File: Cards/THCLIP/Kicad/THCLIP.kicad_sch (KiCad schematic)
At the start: 12 parts, among them J2 Conn_01x03_Pin, J3 Conn_01x05_Pin, K1 Relay_SPDT, U1 RS3K-2424S/H3

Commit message: updated process description more
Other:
- note added: "Process ------- Recieve input height sensing enable signal Activate dc-dc converter - 24V DC will appear on the dc-dc converter output - A small current will flow through via 100 kOhm resistor (shorted output) - Relay will activate - Connection between work piece ground and torch shield ground is broken - Output will be unshorted, current through resistor stops flowing - 23V voltage appears betwe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"
- note removed: "Process ------- Recieve input height sensing signal Activate dc-dc converter - 24V DC will appear on the dc-dc converter output - A small current will flow through via 100 kOhm resistor (shorted output) - Relay will activate - Connection between work piece ground and torch shield ground is broken - Output will be unshorted, current through resistor stops flowing - 23V voltage appears between elec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"
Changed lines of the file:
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@@
 		)
 	)
-	(text "Process\n-------\nRecieve input height sensing signal\nActivate dc-dc converter\n	- 24V DC will appear on the dc-dc converter output\n	- A small current will flow through via 100 kOhm resistor (shorted output)\n	- Relay will activate\n		- Connection between work piece ground and torch shield ground is broken\n		- Output will be unshorted, current through resistor stops flowing\n		- 23V voltage appears between electrode and work piece ground\nWait a few tenths of a second to allow relay to settle before monitoring gap voltage\nWhen Arc voltage < x V: raise contact Signal\nLoss of height sensing signal: exit sensing mode, lower contact Signal\n\n"
+	(text "Process\n-------\nRecieve input height sensing enable signal\nActivate dc-dc converter\n	- 24V DC will appear on the dc-dc converter output\n	- A small current will flow through via 100 kOhm resistor (shorted output)\n	- Relay will activate\n		- Connection between work piece ground and torch shield ground is broken\n		- Output will be unshorted, current through resistor stops flowing\n		- 23V voltage appears between electrode and work piece ground, gap voltage\nWait for gap voltage to go above limit voltage. Needed for relay to settle (some milliseconds)\nWhen gap voltage goes back below limit voltage, that is contact, raise sensed/contact flag\nLoss of enable signal: exit sensing mode, lower contact Signal\n\n"
 		(exclude_from_sim no)
-		(at 88.646 131.826 0)
+		(at 90.424 131.826 0)
 		(effects
 			(font

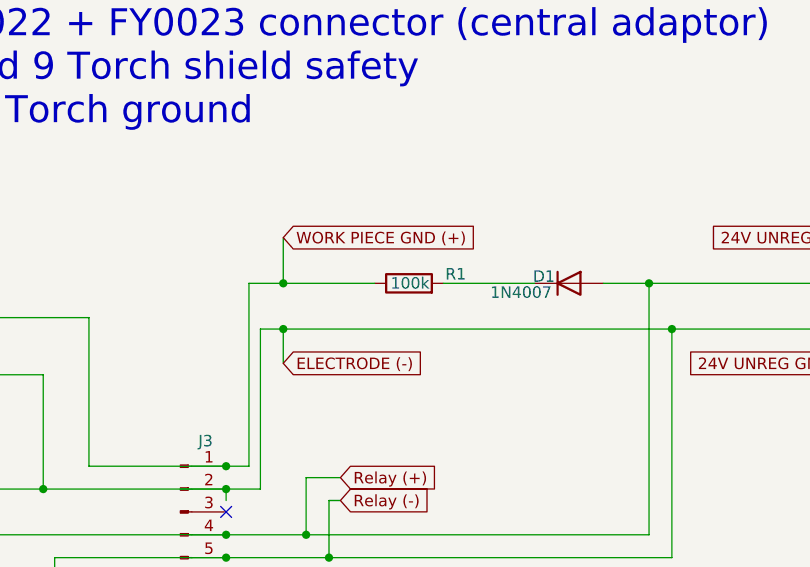
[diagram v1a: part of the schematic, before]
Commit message: Updated short-circuit resistor to 4k7 for more stable voltage.
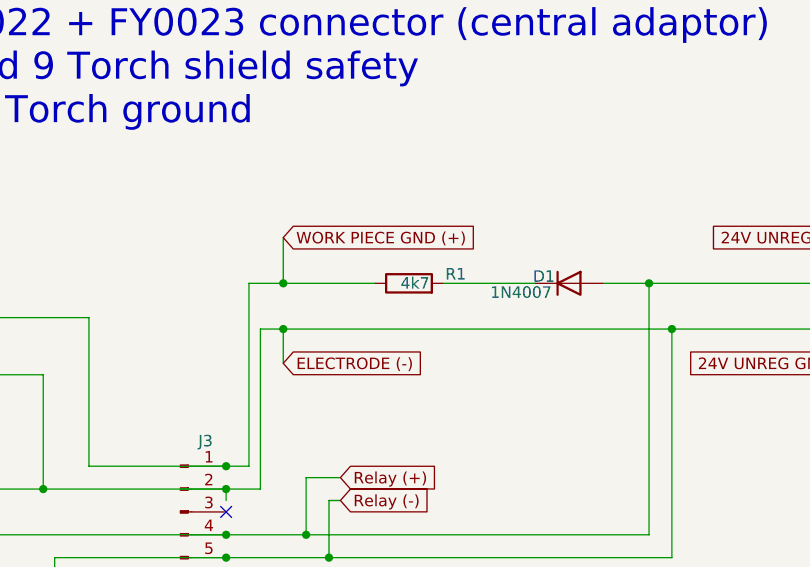
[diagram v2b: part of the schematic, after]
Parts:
- R1: value 100k -> 4k7; footprint Resistor_SMD:R_2512_6332Metric_Pad1.40x3.35mm_HandSolder -> Resistor_THT:R_Axial_DIN0207_L6.3mm_D2.5mm_P10.16mm_Horizontal
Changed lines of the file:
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@@
 			)
 		)
-		(property "Value" "100k"
+		(property "Value" "4k7"
 			(at 152.146 55.88 90)
 			(effects
@@
 			)
 		)
-		(property "Footprint" "Resistor_SMD:R_2512_6332Metric_Pad1.40x3.35mm_HandSolder"
+		(property "Footprint" "Resistor_THT:R_Axial_DIN0207_L6.3mm_D2.5mm_P10.16mm_Horizontal"
 			(at 149.86 57.658 90)
 			(effects

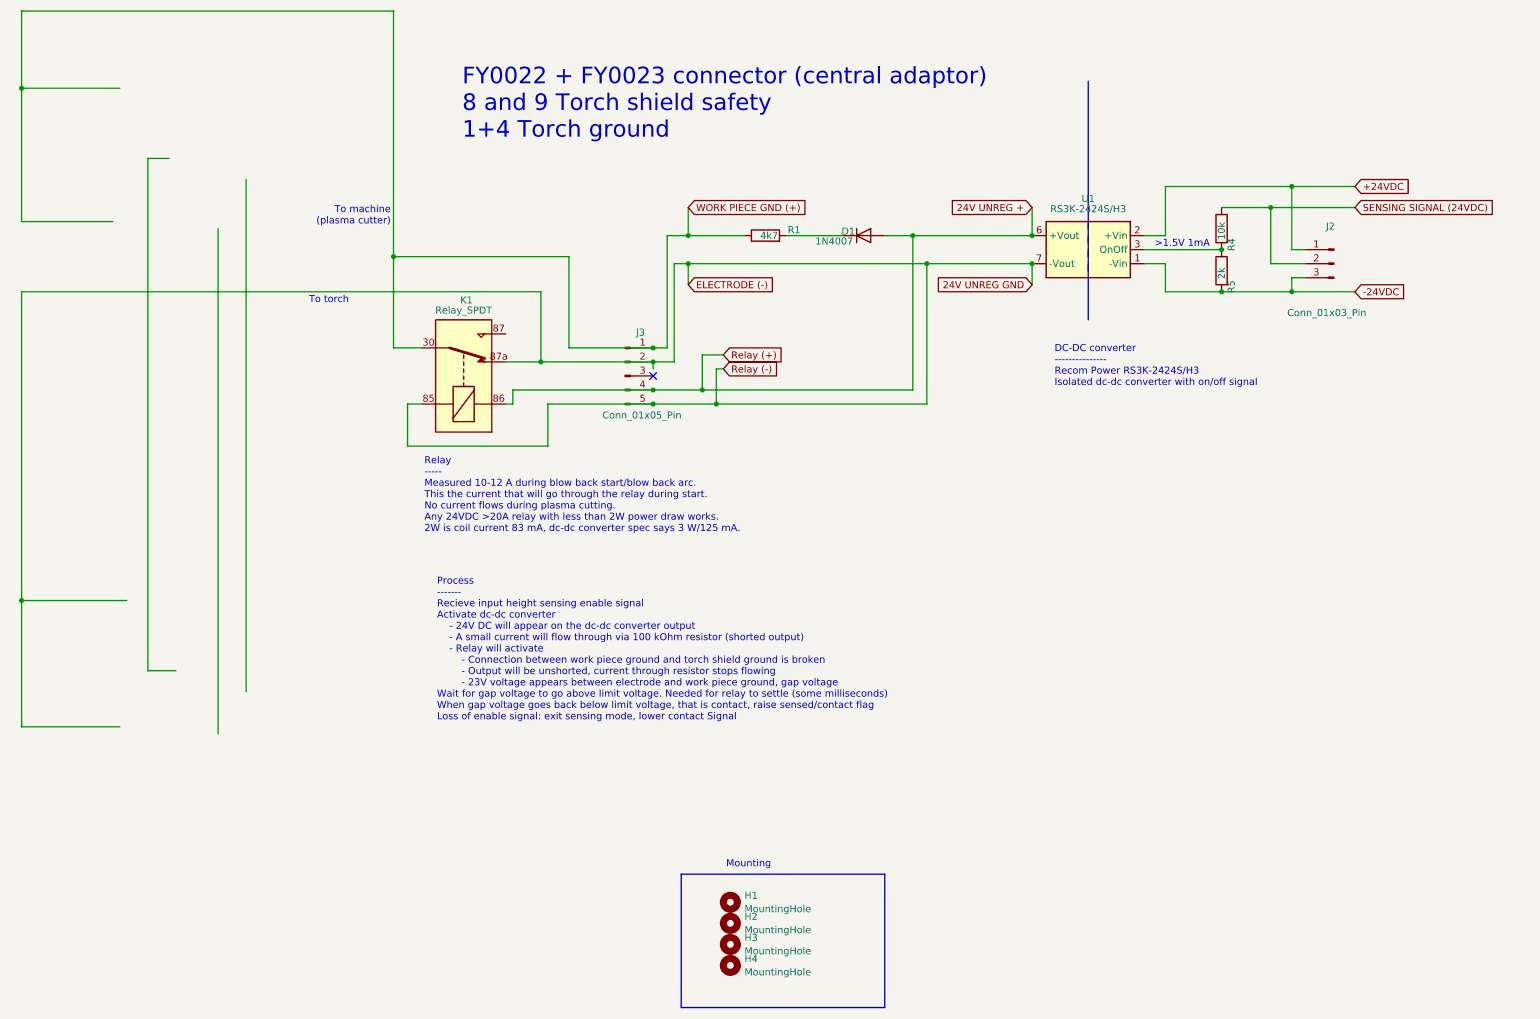
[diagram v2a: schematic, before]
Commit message: Apply voltage on work piece, not torch cable Also read voltage on work piece
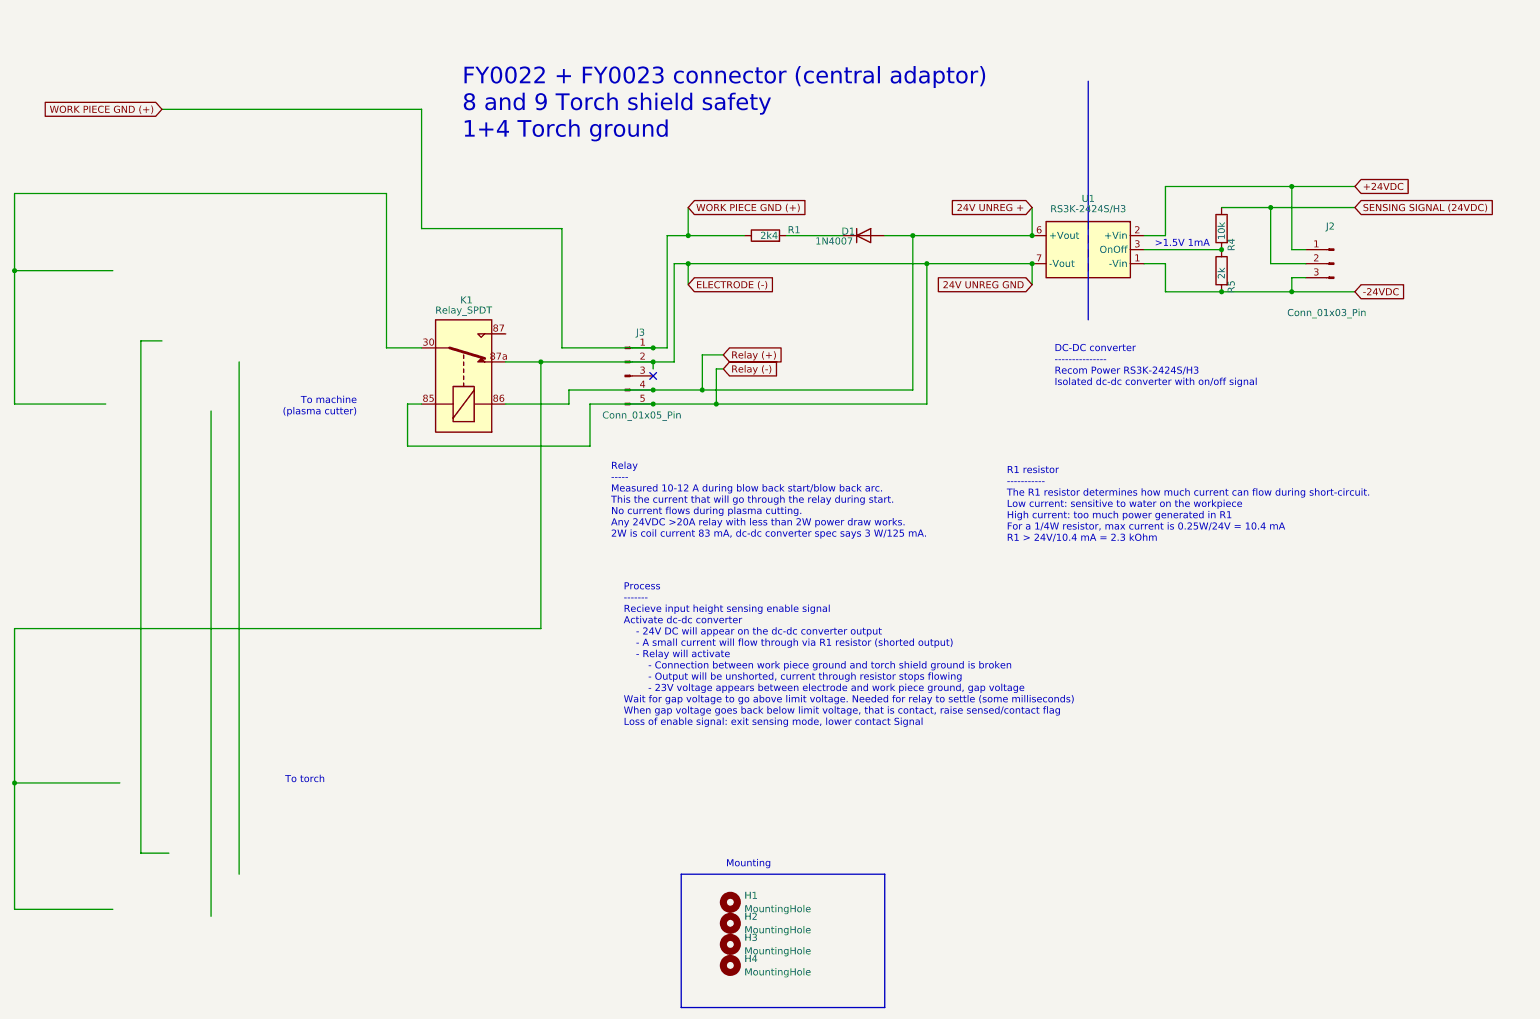
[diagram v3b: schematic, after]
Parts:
- R1: value 4k7 -> 2k4
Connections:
- net WORK PIECE GND (+): no longer K1.30
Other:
- note added: "Process ------- Recieve input height sensing enable signal Activate dc-dc converter - 24V DC will appear on the dc-dc converter output - A small current will flow through via R1 resistor (shorted output) - Relay will activate - Connection between work piece ground and torch shield ground is broken - Output will be unshorted, current through resistor stops flowing - 23V voltage appears between ele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"
- note added: "R1 resistor ----------- The R1 resistor determines how much current can flow during short-circuit. Low current: sensitive to water on the workpiece High current: too much power generated in R1 For a 1/4W resistor, max current is 0.25W/24V = 10.4 mA R1 > 24V/10.4 mA = 2.3 kOhm"
- note removed: "Process ------- Recieve input height sensing enable signal Activate dc-dc converter - 24V DC will appear on the dc-dc converter output - A small current will flow through via 100 kOhm resistor (shorted output) - Relay will activate - Connection between work piece ground and torch shield ground is broken - Output will be unshorted, current through resistor stops flowing - 23V voltage appears betwe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"
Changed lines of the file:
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@@
-	)
-	(junction
-		(at 82.55 59.69)
-		(diameter 0)
-		(color 0 0 0 0)
 	)
 	(junction
@@
 	)
 	(junction
-		(at 15.24 29.21)
+		(at 13.97 62.23)
 		(diameter 0)
 		(color 0 0 0 0)
@@
 	)
 	(junction
-		(at 15.24 121.92)
+		(at 13.97 154.94)
 		(diameter 0)
 		(color 0 0 0 0)
@@
 	(wire
 		(pts
-			(xy 114.3 59.69) (xy 114.3 76.2)
-		)
-		(stroke
-			(width 0)
-			(type dash)
-		)
-	)
-	(wire
-		(pts
-			(xy 114.3 76.2) (xy 129.54 76.2)
-		)
-		(stroke
-			(width 0)
-			(type dash)
-		)
-	)
-	(wire
-		(pts
-			(xy 104.14 83.82) (xy 129.54 83.82)
+			(xy 114.3 83.82) (xy 129.54 83.82)
 		)
 		(stroke
@@
 	(wire
 		(pts
-			(xy 15.24 29.21) (xy 15.24 15.24)
+			(xy 113.03 76.2) (xy 129.54 76.2)
+		)
+		(stroke
+			(width 0)
+			(type dash)
+		)
+	)
+	(wire
+		(pts
+			(xy 13.97 62.23) (xy 13.97 48.26)
 		)
 		(stroke
@@
 	(wire
 		(pts
-			(xy 15.24 121.92) (xy 34.29 121.92)
-		)
-		(stroke
-			(width 0)
-			(type dash)
-		)
-	)
-	(wire
-		(pts
-			(xy 15.24 66.04) (xy 15.24 121.92)
-		)
-		(stroke
-			(width 0)
-			(type dash)
-		)
-	)
-	(wire
-		(pts
-			(xy 55.88 45.72) (xy 55.88 138.43)
-		)
-		(stroke
-			(width 0)
-			(type dash)
-		)
-	)
-	(wire
-		(pts
-			(xy 82.55 76.2) (xy 87.63 76.2)
+			(xy 13.97 154.94) (xy 33.02 154.94)
+		)
+		(stroke
+			(width 0)
+			(type dash)
+		)
+	)
+	(wire
+		(pts
+			(xy 13.97 127) (xy 13.97 154.94)
+		)
+		(stroke
+			(width 0)
+			(type dash)
+		)
+	)
+	(wire
+		(pts
+			(xy 54.61 78.74) (xy 54.61 171.45)
+		)
+		(stroke
+			(width 0)
+			(type dash)
+		)
+	)
+	(wire
+		(pts
+			(xy 81.28 76.2) (xy 87.63 76.2)
 		)
 		(stroke
@@
 	(wire
 		(pts
-			(xy 15.24 15.24) (xy 82.55 15.24)
+			(xy 13.97 48.26) (xy 81.28 48.26)
 		)
 		(stroke
@@
 	(wire
 		(pts
-			(xy 38.1 41.91) (xy 41.91 41.91)
+			(xy 36.83 74.93) (xy 40.64 74.93)
 		)
 		(stroke
@@
 	(wire
 		(pts
-			(xy 15.24 66.04) (xy 109.22 66.04)
+			(xy 13.97 127) (xy 109.22 127)
 		)
 		(stroke
@@
 	(wire
 		(pts
+			(xy 113.03 76.2) (xy 113.03 54.61)
+		)
+		(stroke
+			(width 0)
+			(type dash)
+		)
+	)
+	(wire
+		(pts
 			(xy 135.89 50.8) (xy 135.89 55.88)
 		)
@@
 	(wire
 		(pts
-			(xy 15.24 53.34) (xy 31.75 53.34)
+			(xy 13.97 86.36) (xy 30.48 86.36)
 		)
 		(stroke
@@
 	(wire
 		(pts
-			(xy 38.1 134.62) (xy 43.18 134.62)
+			(xy 36.83 167.64) (xy 41.91 167.64)
 		)
 		(stroke
@@
 	(wire
 		(pts
-			(xy 104.14 83.82) (xy 104.14 86.36)
-		)
-		(stroke
-			(width 0)
-			(type dash)
-		)
-	)
-	(wire
-		(pts
-			(xy 104.14 86.36) (xy 102.87 86.36)
+			(xy 114.3 83.82) (xy 114.3 86.36)
+		)
+		(stroke
+			(width 0)
+			(type dash)
+		)
+	)
+	(wire
+		(pts
+			(xy 114.3 86.36) (xy 102.87 86.36)
 		)
 		(stroke
@@
 	(wire
 		(pts
-			(xy 15.24 144.78) (xy 33.02 144.78)
-		)
-		(stroke
-			(width 0)
-			(type dash)
-		)
-	)
-	(wire
-		(pts
-			(xy 82.55 59.69) (xy 82.55 76.2)
-		)
-		(stroke
-			(width 0)
-			(type dash)
-		)
-	)
-	(wire
-		(pts
-			(xy 15.24 53.34) (xy 15.24 29.21)
-		)
-		(stroke
-			(width 0)
-			(type dash)
-		)
-	)
-	(wire
-		(pts
-			(xy 82.55 59.69) (xy 114.3 59.69)
+			(xy 13.97 177.8) (xy 31.75 177.8)
+		)
+		(stroke
+			(width 0)
+			(type dash)
+		)
+	)
+	(wire
+		(pts
+			(xy 81.28 48.26) (xy 81.28 76.2)
+		)
+		(stroke
+			(width 0)
+			(type dash)
+		)
+	)
+	(wire
+		(pts
+			(xy 13.97 86.36) (xy 13.97 62.23)
 		)
 		(stroke
@@
 	(wire
 		(pts
-			(xy 38.1 41.91) (xy 38.1 134.62)
+			(xy 36.83 74.93) (xy 36.83 167.64)
 		)
 		(stroke
@@
 	(wire
 		(pts
-			(xy 110.49 93.98) (xy 110.49 86.36)
+			(xy 118.11 93.98) (xy 118.11 86.36)
 		)
 		(stroke
@@
 	(wire
 		(pts
+			(xy 87.63 33.02) (xy 40.64 33.02)
+		)
+		(stroke
+			(width 0)
+			(type dash)
+		)
+	)
+	(wire
+		(pts
 			(xy 135.89 60.96) (xy 179.07 60.96)
 		)
@@
 	(wire
 		(pts
-			(xy 85.09 93.98) (xy 110.49 93.98)
-		)
-		(stroke
-			(width 0)
-			(type dash)
-		)
-	)
-	(wire
-		(pts
-			(xy 15.24 121.92) (xy 15.24 144.78)
-		)
-		(stroke
-			(width 0)
-			(type dash)
-		)
-	)
-	(wire
-		(pts
-			(xy 15.24 29.21) (xy 33.02 29.21)
+			(xy 85.09 93.98) (xy 118.11 93.98)
+		)
+		(stroke
+			(width 0)
+			(type dash)
+		)
+	)
+	(wire
+		(pts
+			(xy 13.97 154.94) (xy 13.97 177.8)
+		)
+		(stroke
+			(width 0)
+			(type dash)
+		)
+	)
+	(wire
+		(pts
+			(xy 13.97 62.23) (xy 31.75 62.23)
 		)
 		(stroke
@@
 	(wire
 		(pts
-			(xy 109.22 66.04) (xy 109.22 78.74)
+			(xy 109.22 127) (xy 109.22 78.74)
 		)
 		(stroke
@@
 	(wire
 		(pts
-			(xy 50.8 54.61) (xy 50.8 146.05)
+			(xy 87.63 33.02) (xy 87.63 54.61)
+		)
+		(stroke
+			(width 0)
+			(type dash)
+		)
+	)
+	(wire
+		(pts
+			(xy 49.53 87.63) (xy 49.53 179.07)
+		)
+		(stroke
+			(width 0)
+			(type dash)
+		)
+	)
+	(wire
+		(pts
+			(xy 87.63 54.61) (xy 113.03 54.61)
 		)
 		(stroke
@@
 	(wire
 		(pts
-			(xy 82.55 15.24) (xy 82.55 59.69)
-		)
-		(stroke
-			(width 0)
-			(type dash)
-		)
-	)
-	(wire
-		(pts
-			(xy 110.49 86.36) (xy 129.54 86.36)
+			(xy 118.11 86.36) (xy 129.54 86.36)
 		)
 		(stroke
@@
 	)
 	(image
-		(at 43.815 133.35)
+		(at 42.545 166.37)
 		(scale 2.94325)
 		(data "iVBORw0KGgoAAAANSUhEUgAAAP4AAADpCAYAAAAERYpyAAABhGlDQ1BJQ0MgcHJvZmlsZQAAKJF9"
@@
 	)
 	(image
-		(at 43.18 41.275)
+		(at 41.91 74.295)
 		(scale 2.94325)
 		(data "iVBORw0KGgoAAAANSUhEUgAAAP4AAADpCAYAAAAERYpyAAABhGlDQ1BJQ0MgcHJvZmlsZQAAKJF9"
@@
 		)
 	)
-	(text "Process\n-------\nRecieve input height sensing enable signal\nActivate dc-dc converter\n	- 24V DC will appear on the dc-dc converter output\n	- A small current will flow through via 100 kOhm resistor (shorted output)\n	- Relay will activate\n		- Connection between work piece ground and torch shield ground is broken\n		- Output will be unshorted, current through resistor stops flowing\n		- 23V voltage appears between electrode and work piece ground, gap voltage\nWait for gap voltage to go above limit voltage. Needed for relay to settle (some milliseconds)\nWhen gap voltage goes back below limit voltage, that is contact, raise sensed/contact flag\nLoss of enable signal: exit sensing mode, lower contact Signal\n\n"
+	(text "Process\n-------\nRecieve input height sensing enable signal\nActivate dc-dc converter\n	- 24V DC will appear on the dc-dc converter output\n	- A small current will flow through via R1 resistor (shorted output)\n	- Relay will activate\n		- Connection between work piece ground and torch shield ground is broken\n		- Output will be unshorted, current through resistor stops flowing\n		- 23V voltage appears between electrode and work piece ground, gap voltage\nWait for gap voltage to go above limit voltage. Needed for relay to settle (some milliseconds)\nWhen gap voltage goes back below limit voltage, that is contact, raise sensed/contact flag\nLoss of enable signal: exit sensing mode, lower contact Signal\n\n"
 		(exclude_from_sim no)
-		(at 90.424 131.826 0)
+		(at 124.206 132.842 0)
 		(effects
 			(font
@@
 	(text "To torch"
 		(exclude_from_sim no)
-		(at 70.866 67.564 0)
+		(at 66.548 154.432 0)
 		(effects
 			(font
@@
 	(text "To machine\n(plasma cutter)"
 		(exclude_from_sim no)
-		(at 82.042 50.546 0)
+		(at 75.946 85.09 0)
 		(effects
 			(font
@@
 		)
 	)
+	(text "R1 resistor\n-----------\nThe R1 resistor determines how much current can flow during short-circuit.\nLow current: sensitive to water on the workpiece\nHigh current: too much power generated in R1\nFor a 1/4W resistor, max current is 0.25W/24V = 10.4 mA\nR1 > 24V/10.4 mA = 2.3 kOhm \n\n"
+		(exclude_from_sim no)
+		(at 193.548 105.664 0)
+		(effects
+			(font
+				(size 1.27 1.27)
+			)
+			(justify left)
+		)
+	)
 	(text "DC-DC converter\n---------------\nRecom Power RS3K-2424S/H3\nIsolated dc-dc converter with on/off signal"
 		(exclude_from_sim no)
@@
 	(text "Relay\n-----\nMeasured 10-12 A during blow back start/blow back arc.\nThis the current that will go through the relay during start.\nNo current flows during plasma cutting.\nAny 24VDC >20A relay with less than 2W power draw works.\n2W is coil current 83 mA, dc-dc converter spec says 3 W/125 mA."
 		(exclude_from_sim no)
-		(at 88.138 102.87 0)
+		(at 121.92 103.886 0)
 		(effects
 			(font
@@
 				)
 				(justify left)
+				(hide yes)
+			)
+		)
+	)
+	(global_label "WORK PIECE GND (+)"
+		(shape input)
+		(at 40.64 33.02 180)
+		(fields_autoplaced yes)
+		(effects
+			(font
+				(size 1.27 1.27)
+			)
+			(justify right)
+		)
+		(property "Intersheetrefs" "${INTERSHEET_REFS}"
+			(at 16.851 33.02 0)
+			(effects
+				(font
+					(size 1.27 1.27)
+				)
+				(justify right)
 				(hide yes)
 			)
@@
 			)
 		)
-		(property "Value" "4k7"
+		(property "Value" "2k4"
 			(at 152.146 55.88 90)
 			(effects
